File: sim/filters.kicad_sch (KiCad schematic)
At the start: 45 parts

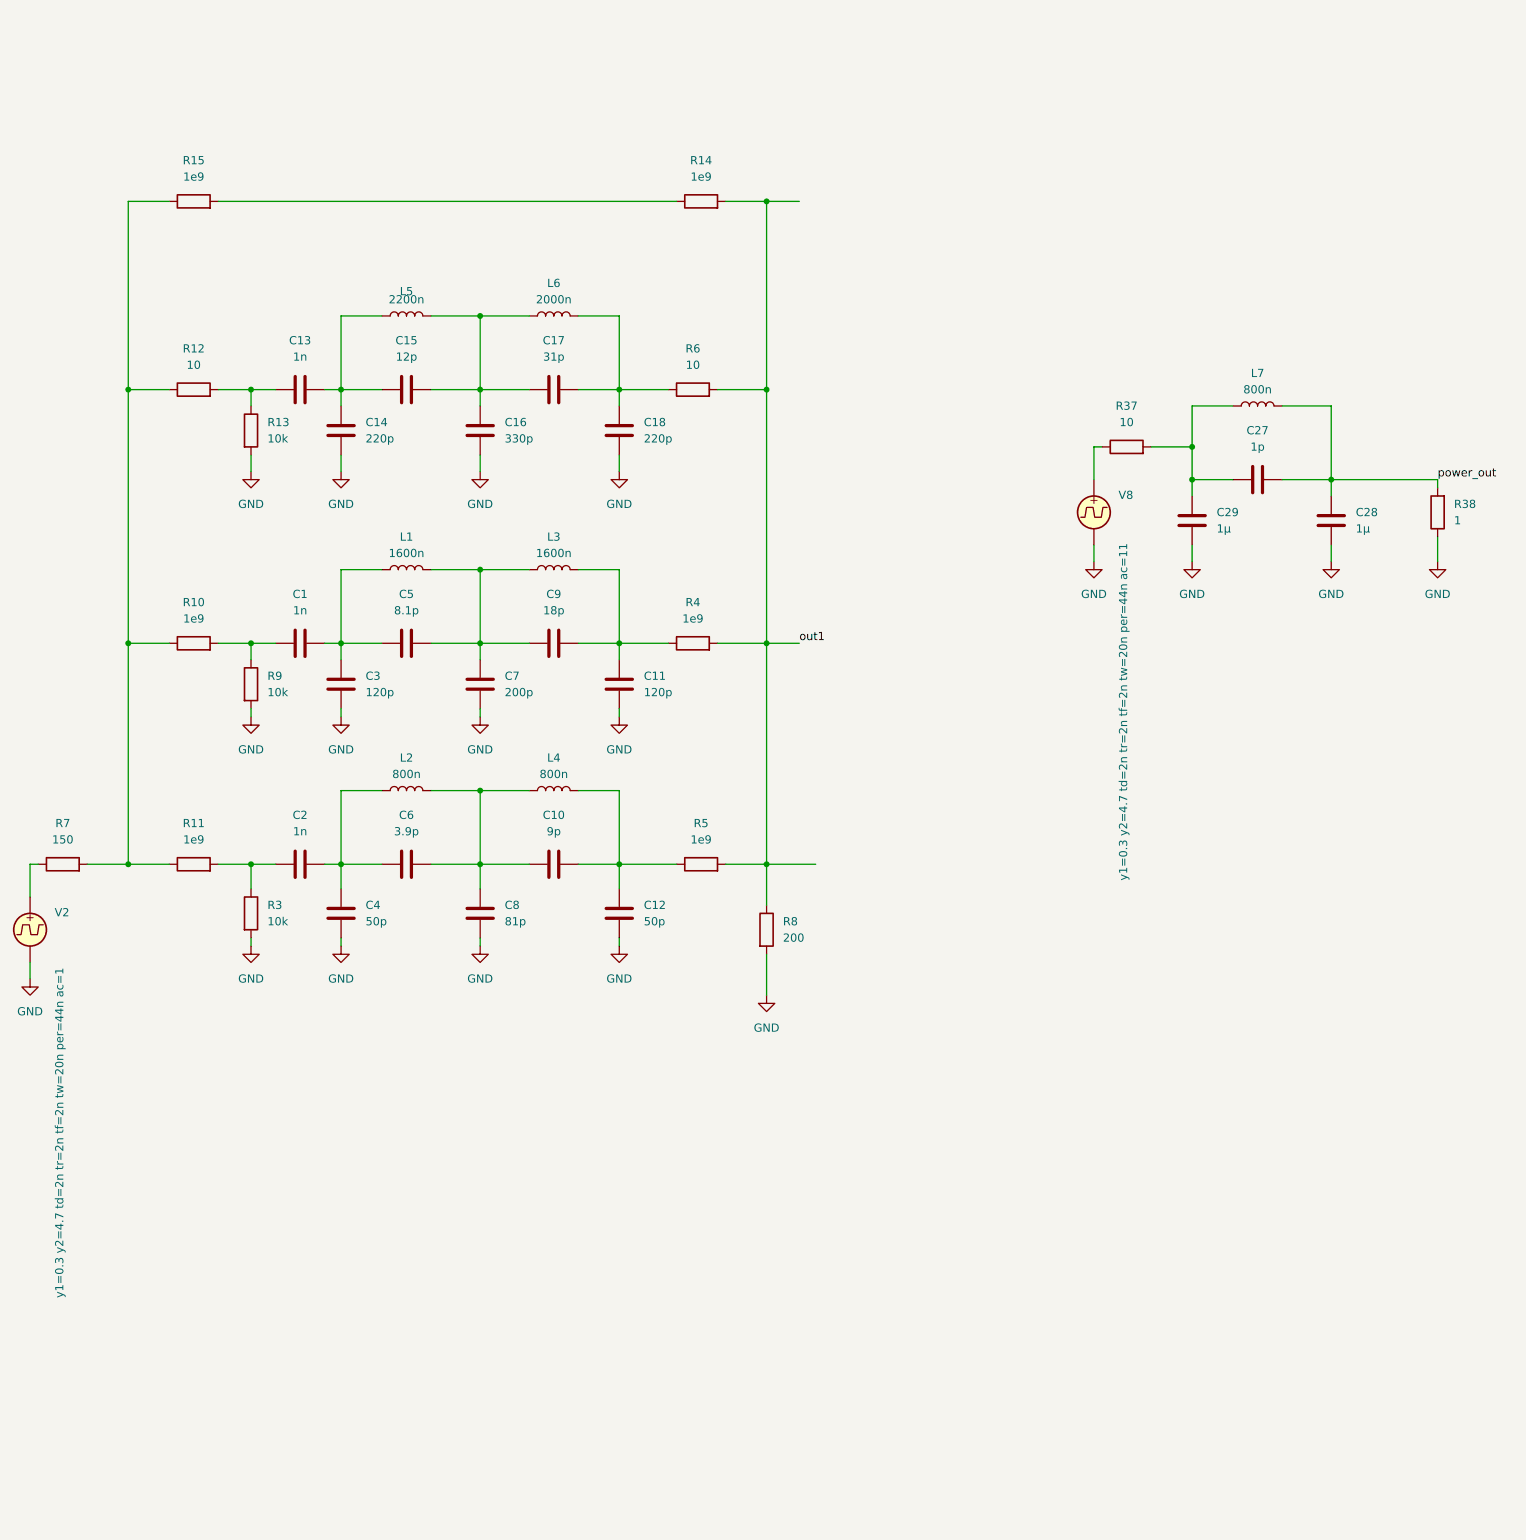
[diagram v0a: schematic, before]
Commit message: Updated filters and improved amp
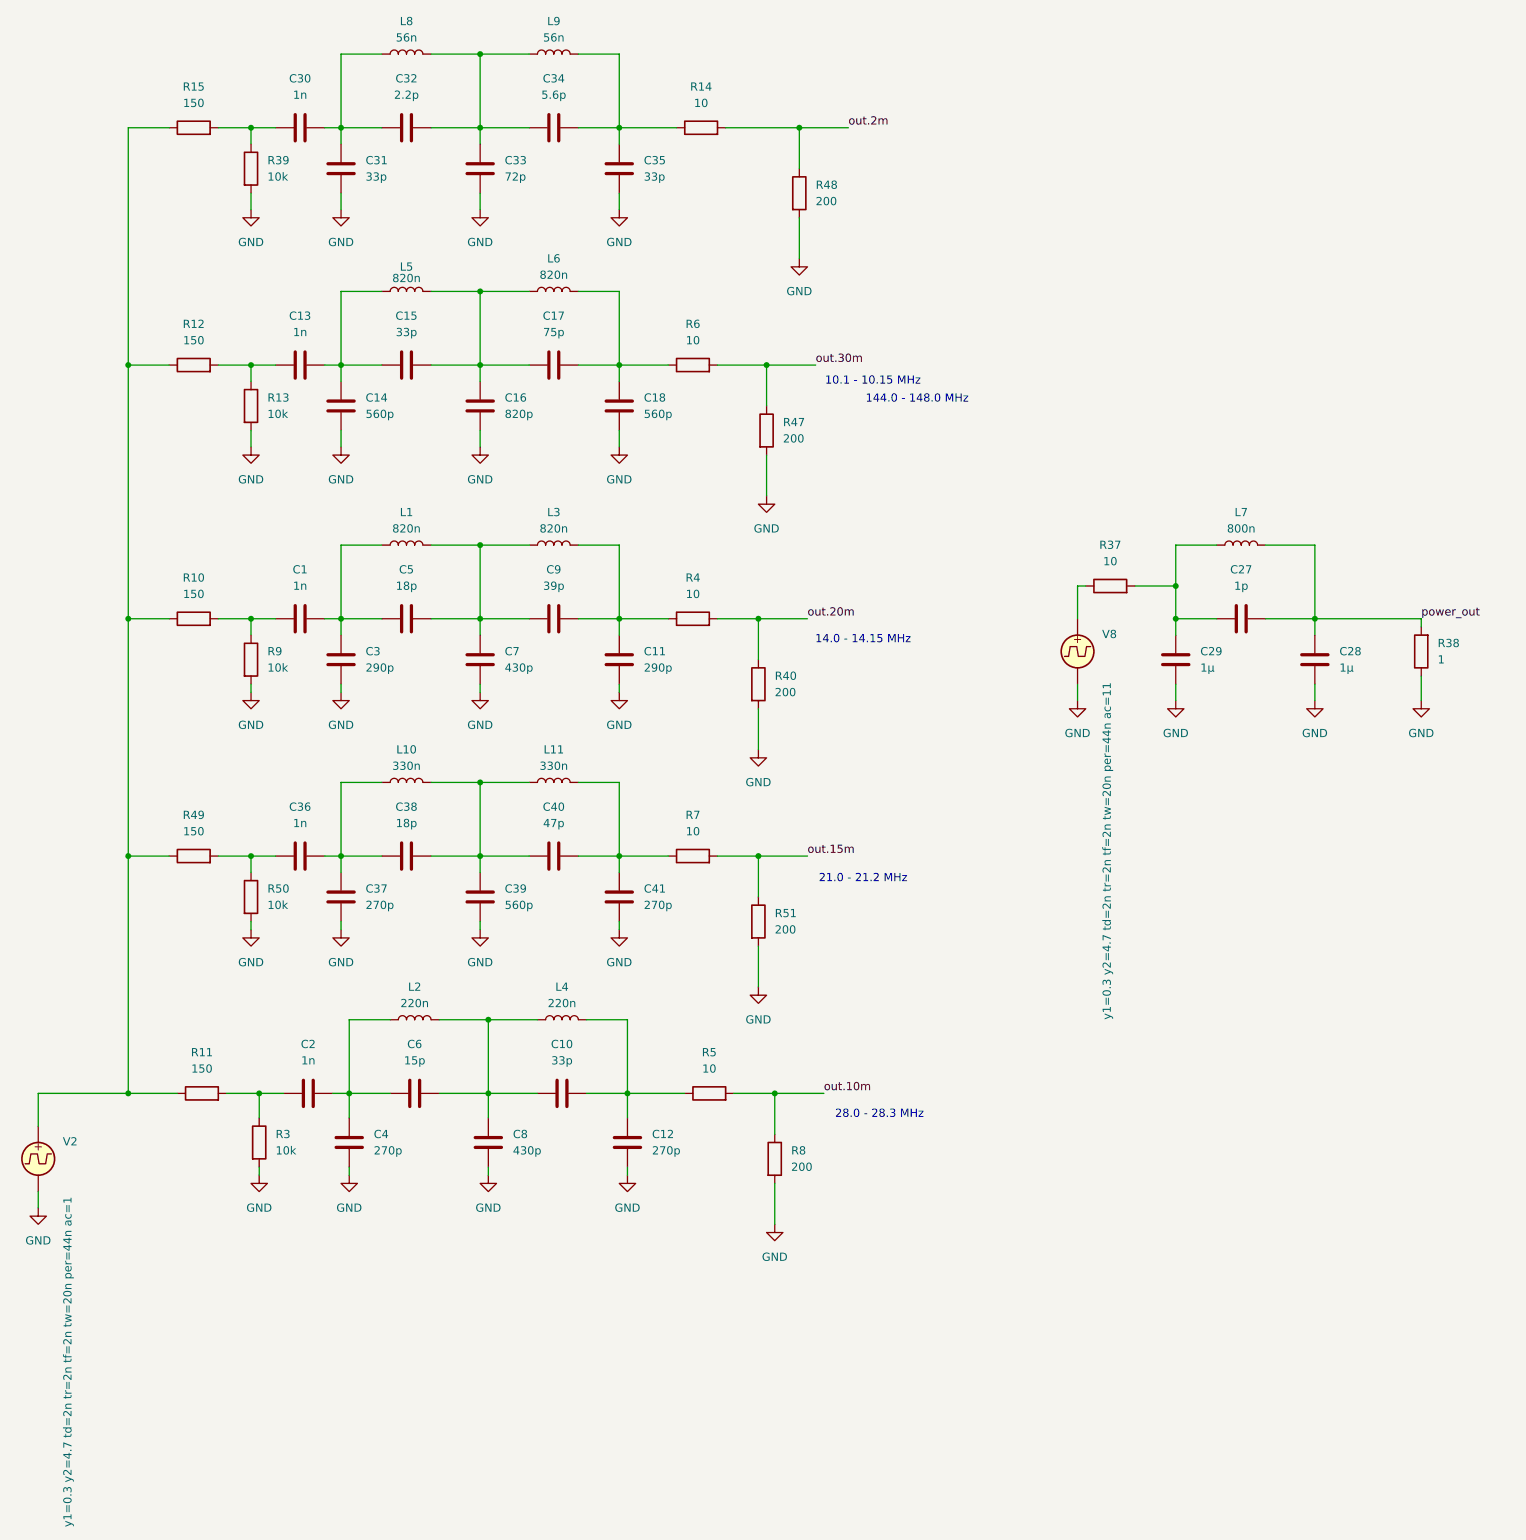
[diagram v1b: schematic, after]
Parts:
- added C30, C36: 1n, symbol Device:C
- added C31, C35: 33p, symbol Device:C
- added C32: 2.2p, symbol Device:C
- added C33: 72p, symbol Device:C
- added C34: 5.6p, symbol Device:C
- added C37, C41: 270p, symbol Device:C
- added C38: 18p, symbol Device:C
- added C39: 560p, symbol Device:C
- added C40: 47p, symbol Device:C
- added L10, L11: 330n, symbol Device:L
- added L8, L9: 56n, symbol Device:L
- added R39, R50: 10k, symbol Device:R
- added R40, R47, R48, R51: 200, symbol Device:R
- added R49: 150, symbol Device:R
- C10: value 9p -> 33p
- C11, C3: value 120p -> 290p
- C12, C4: value 50p -> 270p
- C14, C18: value 220p -> 560p
- C15: value 12p -> 33p
- C16: value 330p -> 820p
- C17: value 31p -> 75p
- C5: value 8.1p -> 18p
- C6: value 3.9p -> 15p
- C7: value 200p -> 430p
- C8: value 81p -> 430p
- C9: value 18p -> 39p
- L1, L3: value 1600n -> 820n
- L2, L4: value 800n -> 220n
- L5: value 2200n -> 820n
- L6: value 2000n -> 820n
- R10, R11, R15: value 1e9 -> 150
- R12: value 10 -> 150
- R14, R4, R5: value 1e9 -> 10
- R7: value 150 -> 10
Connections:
- net GND: now also C31.2, C33.2, C35.2, C37.2, C39.2, C41.2, R39.2, R40.2, R47.2, R48.2, R50.2, R51.2
- net at V2.1: now also R10.1, R11.1, R12.1, R15.1, R49.1; no longer R7.1
- net at R15.2: now also C30.1, R39.1; no longer R14.1
- removed net out1: R14.2, R4.2, R5.2, R6.2, R8.1
- new net: C36.2, C37.1, C38.1, L10.1
- new net: C38.2, C39.1, C40.1, L10.2, L11.1
- new net: C36.1, R49.2, R50.1
- new net: C34.2, C35.1, L9.2, R14.1
- new net: C40.2, C41.1, L11.2, R7.1
- new net: C30.2, C31.1, C32.1, L8.1
- new net: C32.2, C33.1, C34.1, L8.2, L9.1
- new net out.10m: R5.2, R8.1
- new net out.15m: R51.1, R7.2
- new net out.20m: R4.2, R40.1
- new net out.2m: R14.2, R48.1
- new net out.30m: R47.1, R6.2
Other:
- note added: "10.1 - 10.15 MHz"
- note added: "14.0 - 14.15 MHz"
- note added: "144.0 - 148.0 MHz"
- note added: "21.0 - 21.2 MHz"
- note added: "28.0 - 28.3 MHz"
- moved on the sheet: C1, C10, C11, C12, C13, C14, C15, C16, C17, C18, C2, C27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
